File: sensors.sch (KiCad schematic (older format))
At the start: 13 parts, among them U6 ICM-20948, U7 BMP388

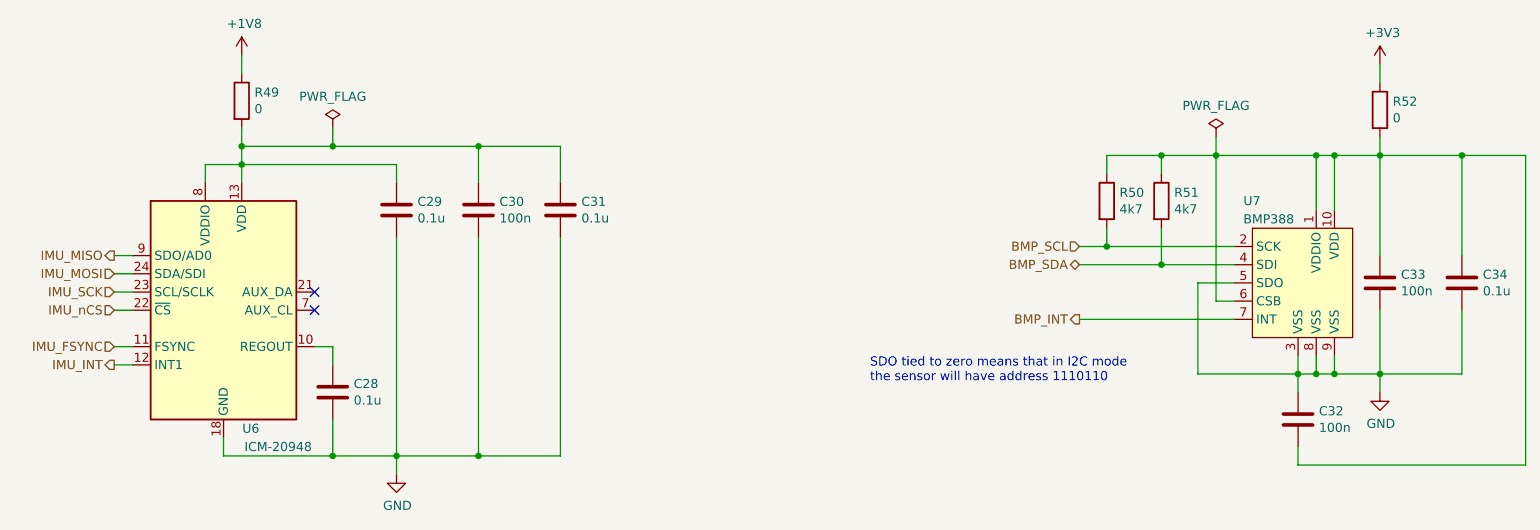
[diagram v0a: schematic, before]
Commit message: Add 10k pull-downs on MCU LED outputs, improve layout
Pushed few traces, fixed DRC issue on one of the vias.
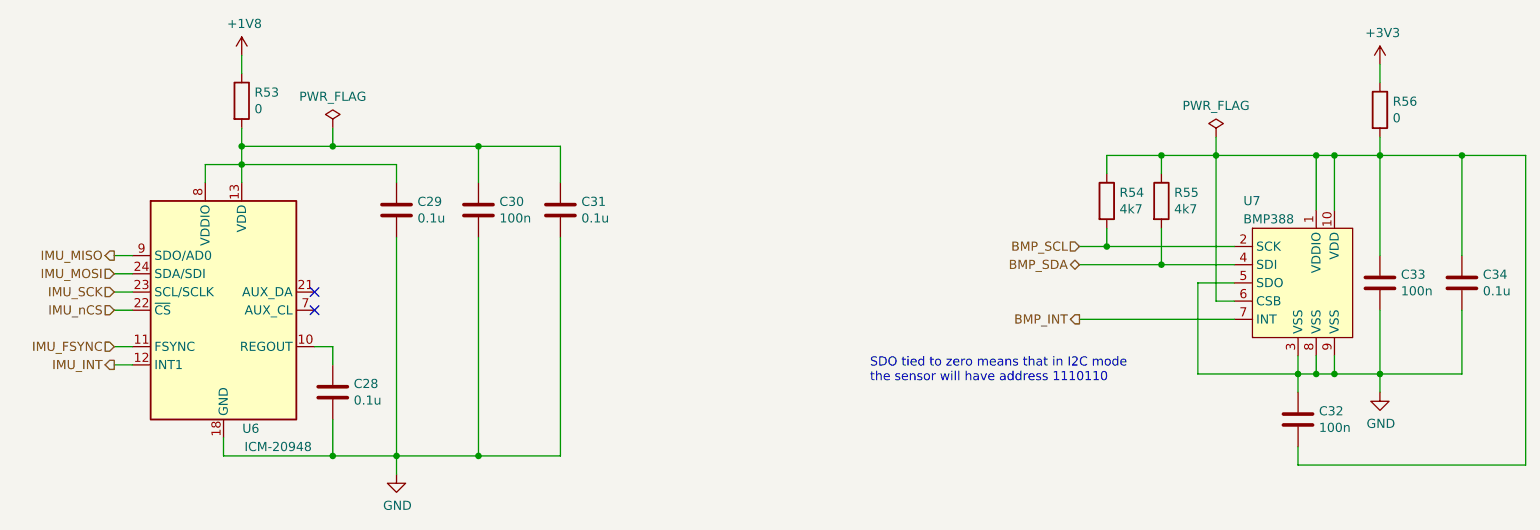
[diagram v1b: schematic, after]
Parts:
- renumbered R49 to R53, R50 to R54, R51 to R55, R52 to R56
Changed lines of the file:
@@
 $EndComp
 $Comp
-L Device:R R51
+L Device:R R55
 U 1 1 5E4A4DD8
 P 7900 3050
-F 0 "R51" H 7970 3096 50  0000 L CNN
+F 0 "R55" H 7970 3096 50  0000 L CNN
 F 1 "4k7" H 7970 3005 50  0000 L CNN
 F 2 "Resistor_SMD:R_0603_1608Metric_Pad1.05x0.95mm_HandSolder" V 7830 3050 50  0001 C CNN
@@
 $EndComp
 $Comp
-L Device:R R50
+L Device:R R54
 U 1 1 5E4A517E
 P 7600 3050
-F 0 "R50" H 7670 3096 50  0000 L CNN
+F 0 "R54" H 7670 3096 50  0000 L CNN
 F 1 "4k7" H 7670 3005 50  0000 L CNN
 F 2 "Resistor_SMD:R_0603_1608Metric_Pad1.05x0.95mm_HandSolder" V 7530 3050 50  0001 C CNN
@@
 	9100 4000 9100 4100
 $Comp
-L Device:R R52
+L Device:R R56
 U 1 1 5EC5840F
 P 9100 2550
-F 0 "R52" H 9170 2596 50  0000 L CNN
+F 0 "R56" H 9170 2596 50  0000 L CNN
 F 1 "0" H 9170 2505 50  0000 L CNN
 F 2 "Resistor_SMD:R_0603_1608Metric_Pad1.05x0.95mm_HandSolder" V 9030 2550 50  0001 C CNN
@@
 IMU_nCS
 $Comp
-L Device:R R49
+L Device:R R53
 U 1 1 5EC713A7
 P 2850 2500
-F 0 "R49" H 2920 2546 50  0000 L CNN
+F 0 "R53" H 2920 2546 50  0000 L CNN
 F 1 "0" H 2920 2455 50  0000 L CNN
 F 2 "Resistor_SMD:R_0603_1608Metric_Pad1.05x0.95mm_HandSolder" V 2780 2500 50  0001 C CNN
@@
 	2150 3650 2250 3650
 $Comp
-L power:PWR_FLAG #FLG07
+L power:PWR_FLAG #FLG08
 U 1 1 5E3AD934
 P 8200 2700
-F 0 "#FLG07" H 8200 2775 50  0001 C CNN
+F 0 "#FLG08" H 8200 2775 50  0001 C CNN
 F 1 "PWR_FLAG" H 8200 2873 50  0000 C CNN
 F 2 "" H 8200 2700 50  0001 C CNN
@@
 $EndComp
 $Comp
-L power:PWR_FLAG #FLG06
+L power:PWR_FLAG #FLG07
 U 1 1 5E3AF8FB
 P 3350 2650
-F 0 "#FLG06" H 3350 2725 50  0001 C CNN
+F 0 "#FLG07" H 3350 2725 50  0001 C CNN
 F 1 "PWR_FLAG" H 3350 2823 50  0000 C CNN
 F 2 "" H 3350 2650 50  0001 C CNN
@@
 	8200 2700 8200 2800
 $Comp
-L power:+1V8 #PWR0101
+L power:+1V8 #PWR058
 U 1 1 5E7177C3
 P 2850 2250
-F 0 "#PWR0101" H 2850 2100 50  0001 C CNN
+F 0 "#PWR058" H 2850 2100 50  0001 C CNN
 F 1 "+1V8" H 2865 2423 50  0000 C CNN
 F 2 "" H 2850 2250 50  0001 C CNN

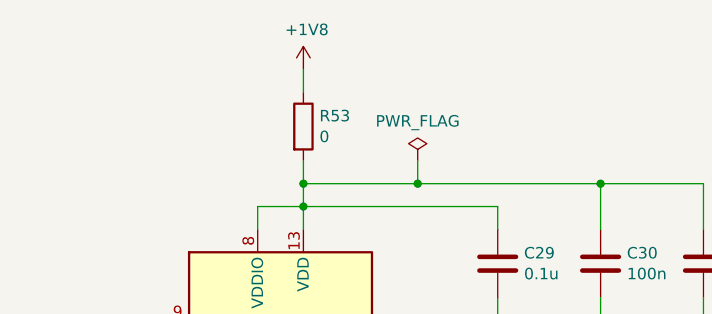
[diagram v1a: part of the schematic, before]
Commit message: Change ICM-20948 supply from 1V8 to 3V3
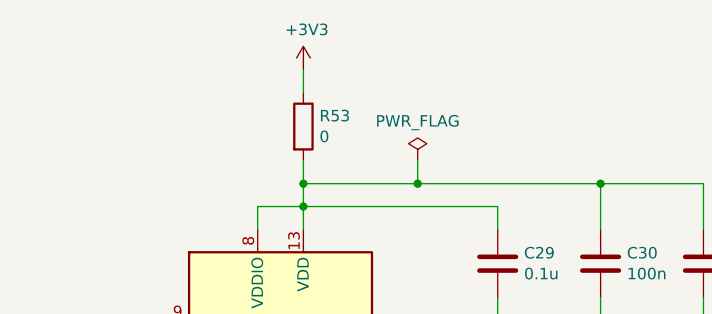
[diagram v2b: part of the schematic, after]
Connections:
- net +1V8 is gone; now on net +3V3: R53.1
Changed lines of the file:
@@
 	8200 2700 8200 2800
 $Comp
-L power:+1V8 #PWR058
-U 1 1 5E7177C3
+L power:+3V3 #PWR?
+U 1 1 5EBE51D4
 P 2850 2250
-F 0 "#PWR058" H 2850 2100 50  0001 C CNN
-F 1 "+1V8" H 2865 2423 50  0000 C CNN
+F 0 "#PWR?" H 2850 2100 50  0001 C CNN
+F 1 "+3V3" H 2865 2423 50  0000 C CNN
 F 2 "" H 2850 2250 50  0001 C CNN
 F 3 "" H 2850 2250 50  0001 C CNN
